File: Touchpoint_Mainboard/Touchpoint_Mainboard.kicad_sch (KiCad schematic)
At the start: 48 parts, among them J2 Conn_01x02, SW1 SW_SPST, SW2 SW_SPST, SW3 SW_SPST, U4 NCP1117-3.3_SOT223, U5 W25Q128JVS, U6 RP2040, Y1 ABM8-272-T3

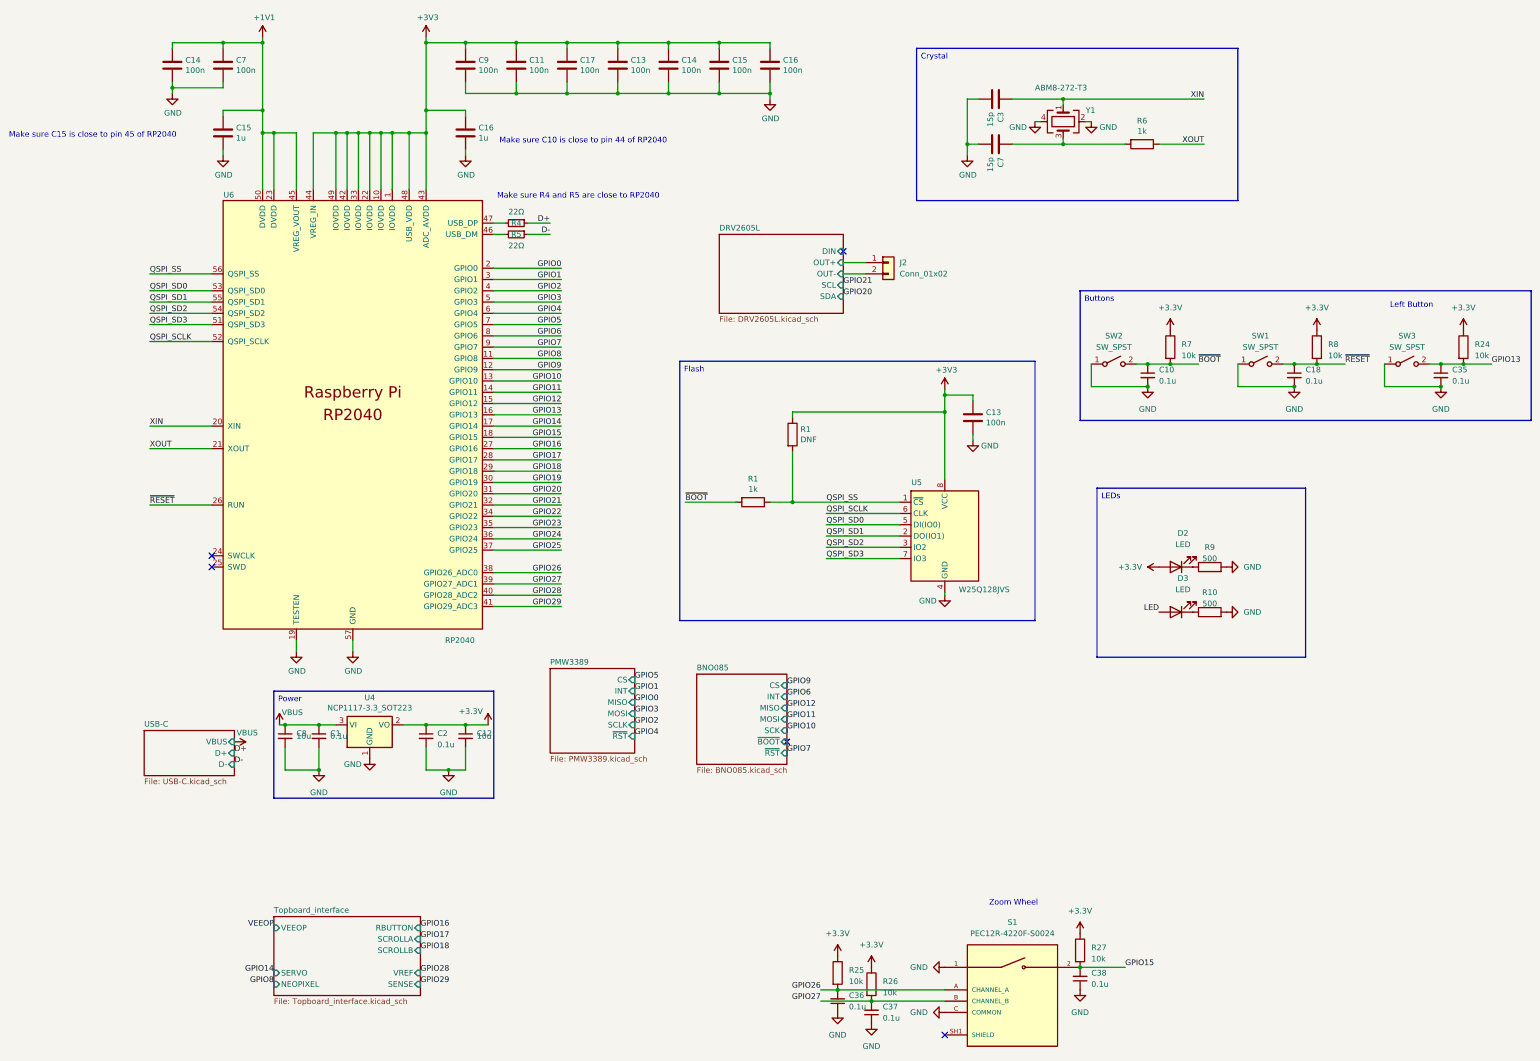
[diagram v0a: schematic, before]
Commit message: FInished populating mainboard schematic
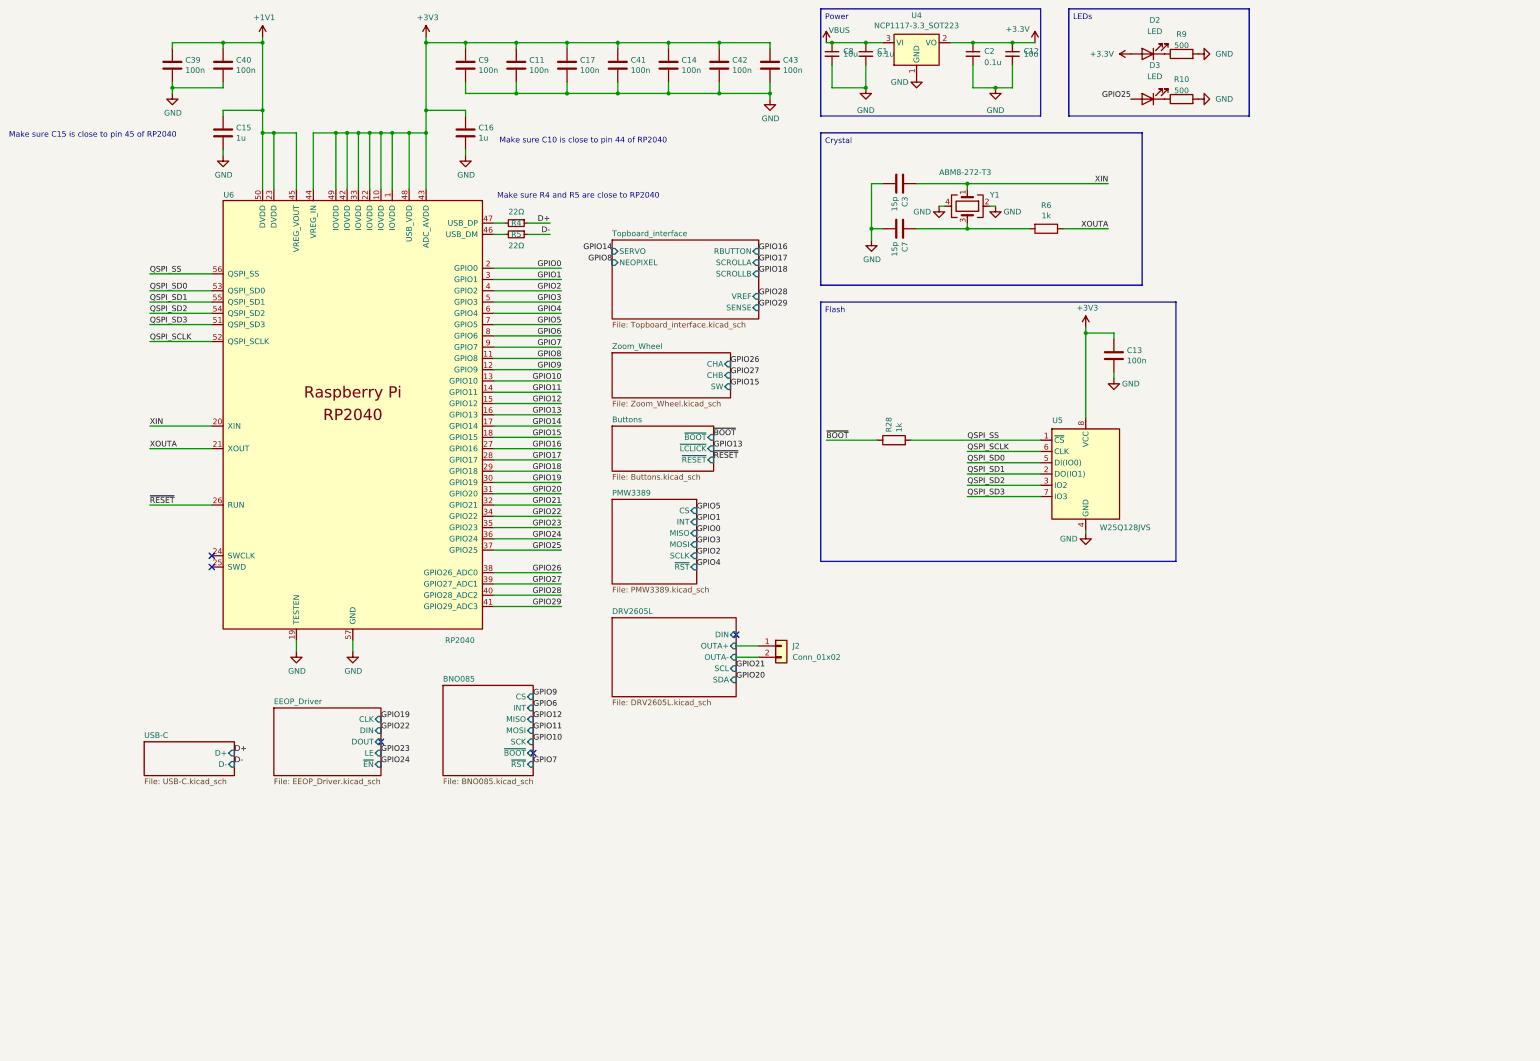
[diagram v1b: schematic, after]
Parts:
- removed C10, C18, C35, C36, C37, C38: 0.1u, Capacitor_SMD:C_0402_1005Metric, symbol Device:C_Small
- removed C13, C14, C15, C16, C7: 100n, Capacitor_SMD:C_0402_1005Metric, symbol Device:C
- removed R1: 1k, Resistor_SMD:R_0402_1005Metric, symbol Device:R
- removed R1: DNF, Resistor_SMD:R_0402_1005Metric, symbol Device:R
- removed R24, R25, R26, R27, R7, R8: 10k, Resistor_SMD:R_0402_1005Metric, symbol Device:R
- removed S1: PEC12R-4220F-S0024, PEC12R-4220F-S0024:XDCR_PEC12R-4220F-S0024, symbol PEC12R-4220F-S0024:PEC12R-4220F-S0024
- removed SW1, SW2, SW3: SW_SPST, Button_Switch_THT:SW_PUSH_6mm, symbol Switch:SW_SPST
- added C39, C40, C41, C42, C43: 100n, Capacitor_SMD:C_0402_1005Metric, symbol Device:C
- added R28: 1k, Resistor_SMD:R_0402_1005Metric, symbol Device:R
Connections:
- net LED is gone; now on net GPIO25: D3.2 (A)
- net +1V1: now also C39.1, C40.1
- net +3V3: now also C41.1, C42.1, C43.1
- net GND: now also C39.2, C40.2, C41.2, C42.2, C43.2
- net QSPI_SS: now also R28.2
- net ~{BOOT}: now also R28.1
- net DRV2605L/OUT+ renamed DRV2605L/OUTA+
- net DRV2605L/OUT- renamed DRV2605L/OUTA-
- net XOUT renamed XOUTA
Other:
- added sheet Buttons (Buttons.kicad_sch)
- added sheet EEOP_Driver (EEOP_Driver.kicad_sch)
- added sheet Zoom_Wheel (Zoom_Wheel.kicad_sch)
- sheet DRV2605L ports: added OUTA+, OUTA-; removed OUT+, OUT-
- sheet Topboard_interface ports: added none; removed VEEOP
- sheet USB-C ports: added none; removed VBUS
- note removed: "Left Button"
- note removed: "Zoom Wheel"
- moved on the sheet: C1, C12, C13, C2, C3, C7, C8, D2, D3, J2, R10, R6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

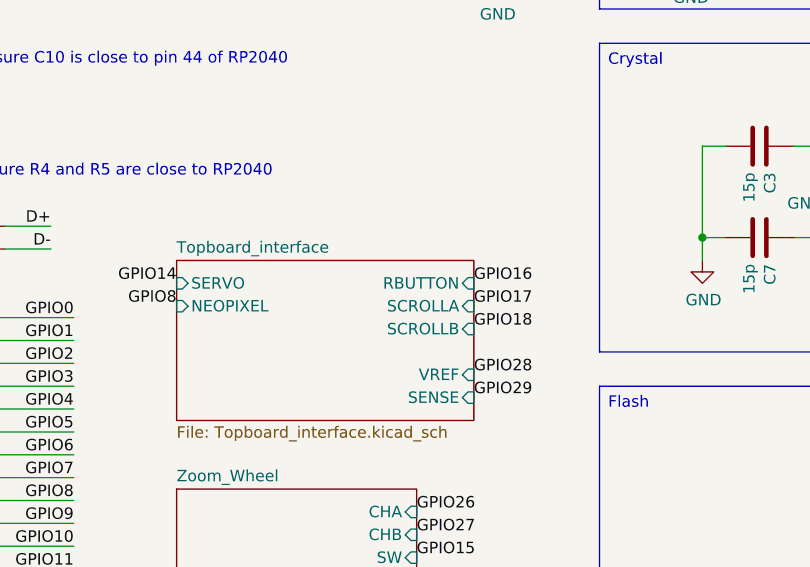
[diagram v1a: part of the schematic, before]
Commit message: Added remaining interface things to topboard schematic
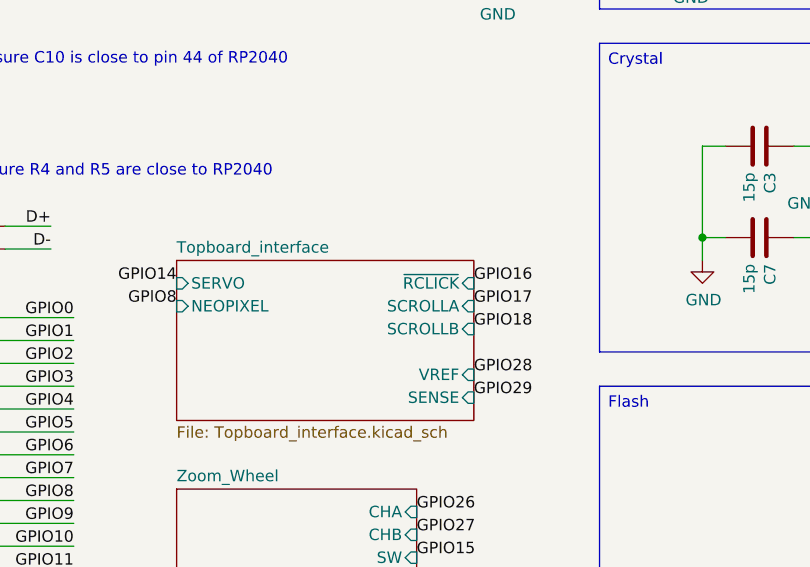
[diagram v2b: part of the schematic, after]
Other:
- sheet Topboard_interface ports: added ~{RCLICK}; removed RBUTTON
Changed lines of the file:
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@@
 			)
 		)
-		(pin "RBUTTON" input
+		(pin "~{RCLICK}" input
 			(at 156.21 71.12 0)
 			(effects

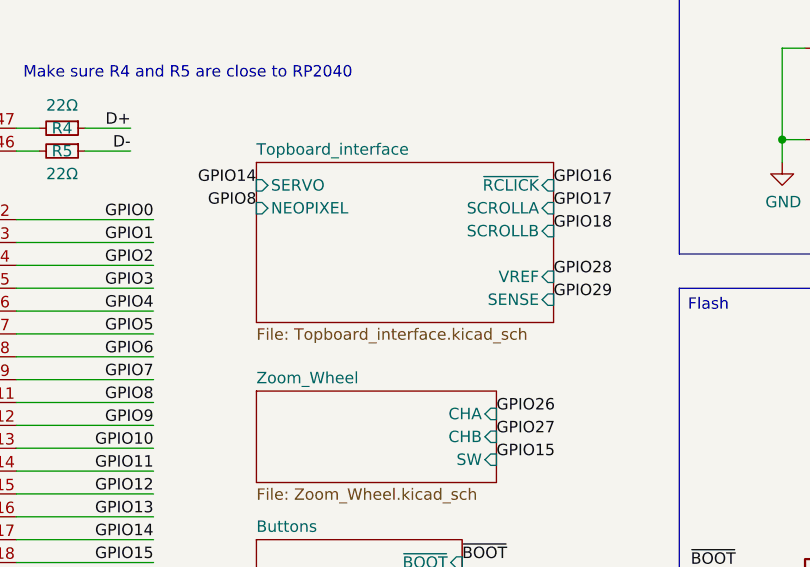
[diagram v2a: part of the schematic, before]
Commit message: Finished assigning most footprints
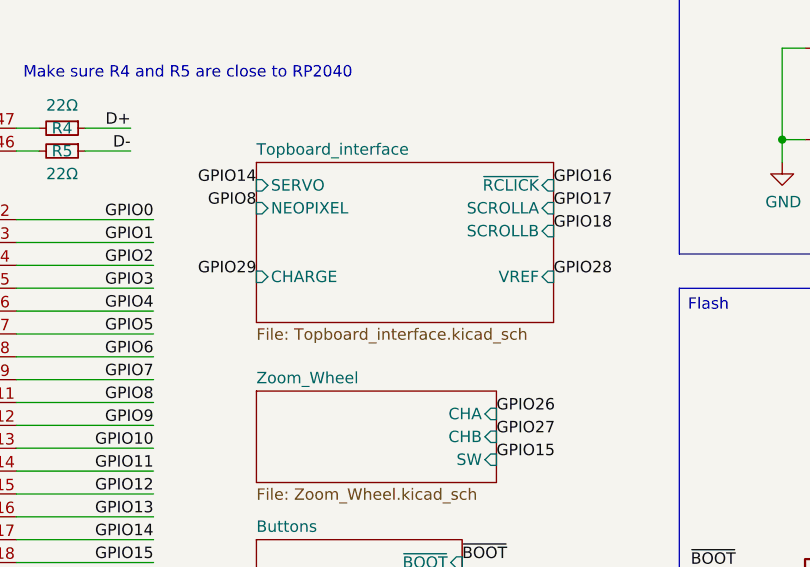
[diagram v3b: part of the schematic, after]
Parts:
- J2: footprint (none) -> Connector_Wire:SolderWire-0.1sqmm_1x02_P3.6mm_D0.4mm_OD1mm
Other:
- sheet Topboard_interface ports: added CHARGE; removed SENSE
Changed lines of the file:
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@@
 	)
 	(label "GPIO29"
-		(at 156.21 83.82 0)
+		(at 123.19 81.28 180)
 		(effects
 			(font
 				(size 1.27 1.27)
 			)
-			(justify left bottom)
+			(justify right bottom)
 		)
 	)
@@
 			)
 		)
-		(property "Footprint" ""
+		(property "Footprint" "Connector_Wire:SolderWire-0.1sqmm_1x02_P3.6mm_D0.4mm_OD1mm"
 			(at 161.29 160.02 0)
 			(effects
@@
 			)
 		)
-		(pin "SENSE" input
-			(at 156.21 83.82 0)
+		(pin "CHARGE" input
+			(at 123.19 81.28 180)
 			(effects
 				(font
 					(size 1.27 1.27)
 				)
-				(justify right)
+				(justify left)
 			)
 		)

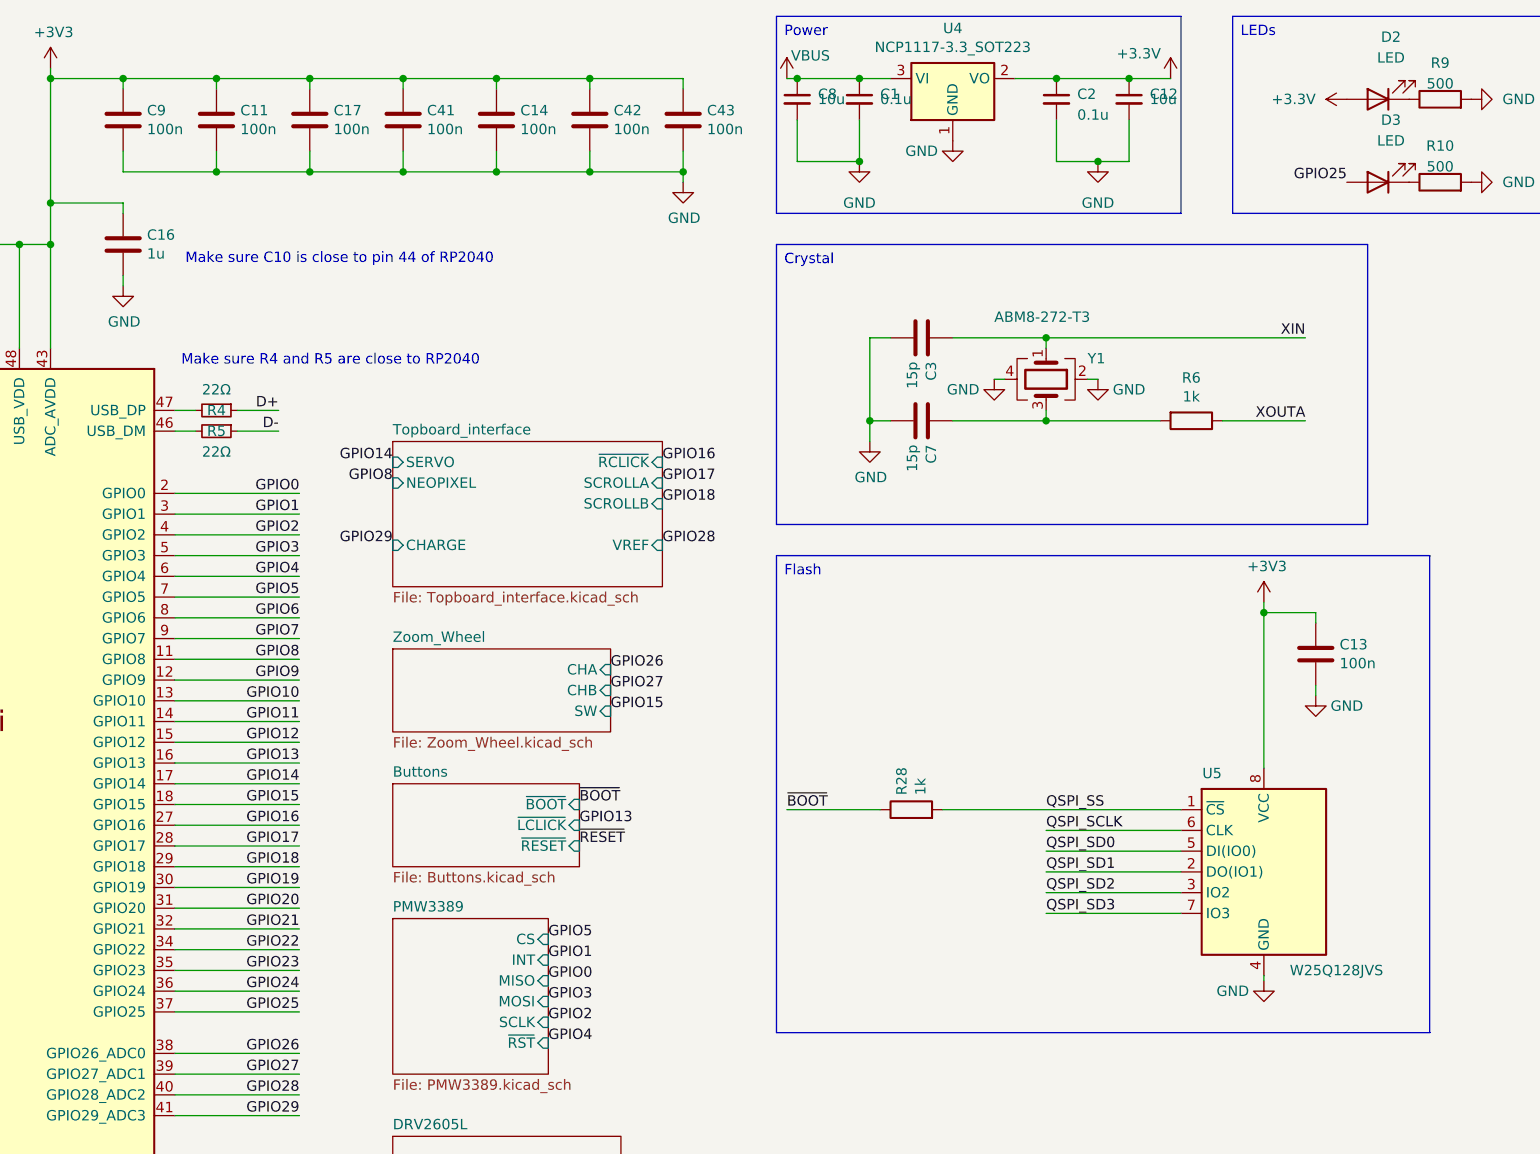
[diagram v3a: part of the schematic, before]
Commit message: Changed some component values based on availability
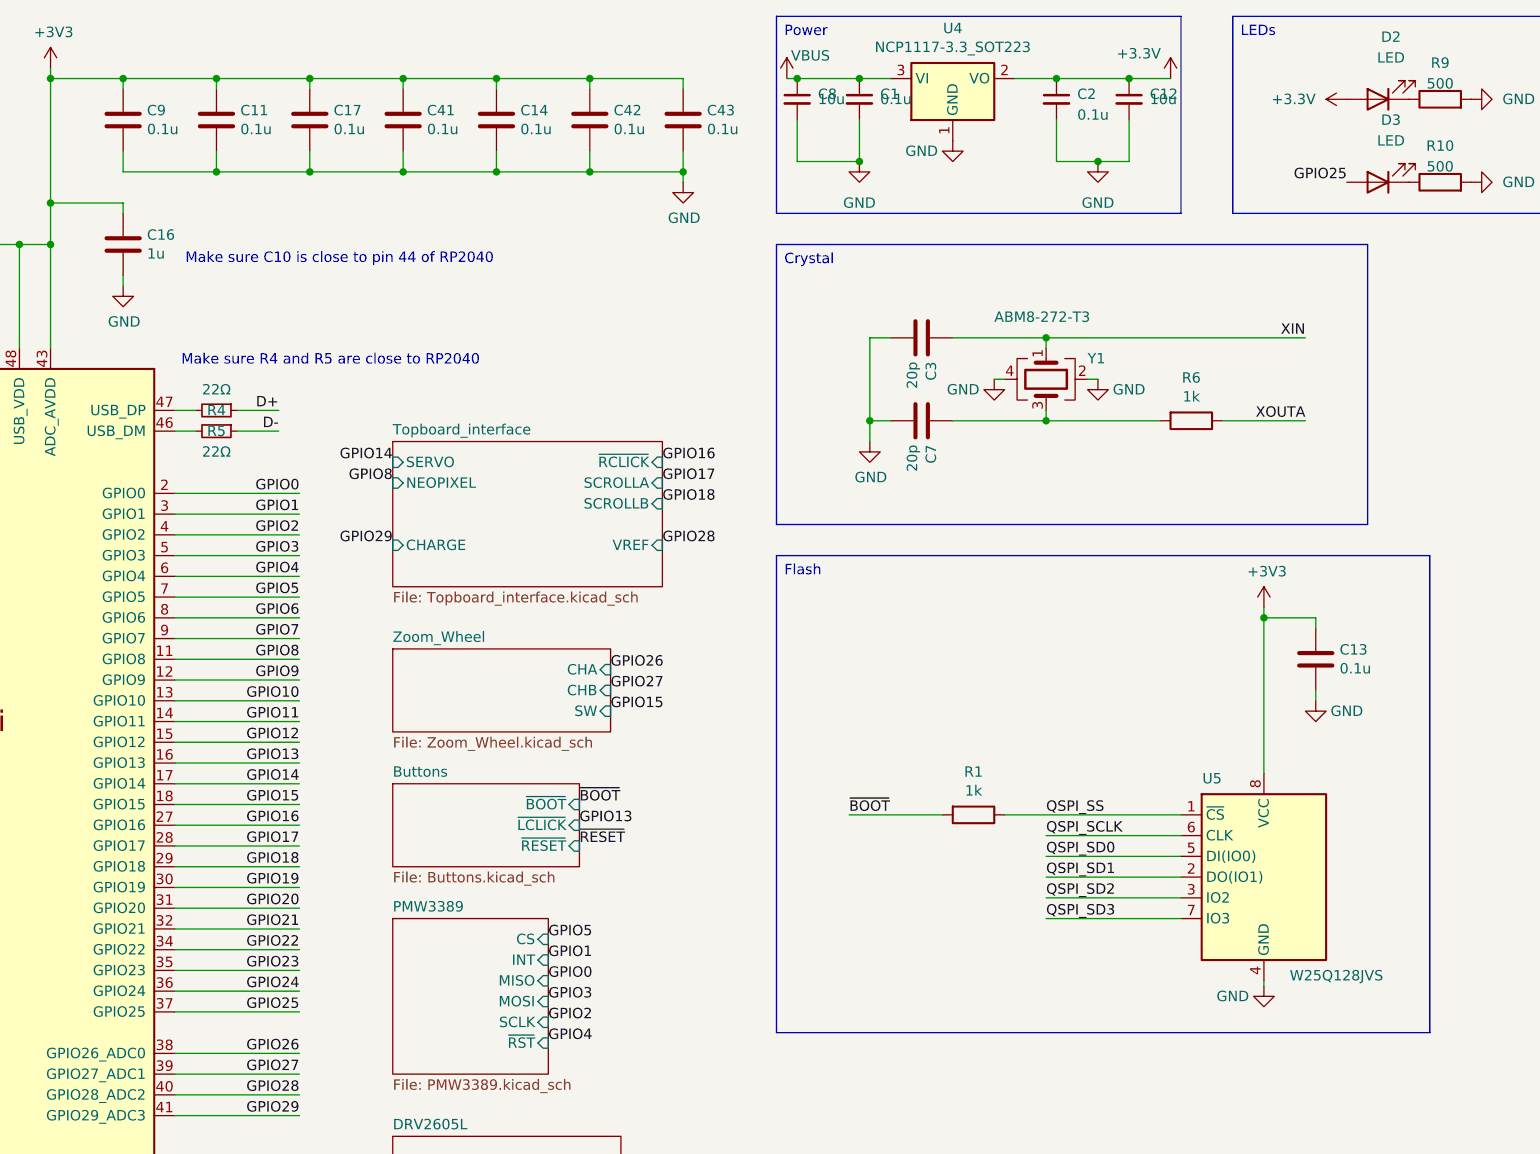
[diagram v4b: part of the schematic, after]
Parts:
- removed R28: 1k, Resistor_SMD:R_0402_1005Metric, symbol Device:R
- added R1: 1k, Resistor_SMD:R_0402_1005Metric, symbol Device:R
- C11, C13, C14, C17, C41, C42, C43, C9: value 100n -> 0.1u
- C3, C7: value 15p -> 20p
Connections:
- net QSPI_SS: now also R1.1
- net ~{BOOT}: now also R1.2
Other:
- moved on the sheet: C13, U5
